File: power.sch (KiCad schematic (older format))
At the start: 3 parts

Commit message: LiPo recharge circuit
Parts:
- added C? (x2): 4.7u, symbol C
- added D?: LED, symbol LED
- added D?: MBRA140, symbol D_Schottky_Small
- added R?: 330, symbol R
- added R?: 2k, symbol R
- added U?: MCP73831, symbol MCP73831
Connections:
- net labels added: +BATT, V_USB
- wire segments 8 -> 27
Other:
- note added: "Allows to recharge \na 1 cell LiPo at 500mA\n\nIreg = 1000V/Rprog"
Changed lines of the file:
@@
 $EndComp
 Wire Wire Line
-	7600 1850 7600 1950
+	7600 1850 7600 1900
+Wire Wire Line
+	7600 1900 7600 1950
 Wire Wire Line
 	7600 1900 8150 1900
@@
 	9550 1950 9550 1900
 Wire Wire Line
-	9350 1900 9750 1900
+	9350 1900 9550 1900
+Wire Wire Line
+	9550 1900 9750 1900
 NoConn ~ 9350 2100
 Text Label 8100 2100 2    39   ~ 0
@@
 Text Notes 8200 1550 0    39   ~ 0
 3.3V to 2.8V linear regulator\nUsed to power the TOF sensor VL6180\nSee sensors sheet
+$Comp
+L MCP73831 U?
+U 1 1 5537ACF5
+P 3650 2050
+F 0 "U?" H 3400 1800 60  0000 C CNN
+F 1 "MCP73831" H 3650 2300 60  0000 C CNN
+F 2 "" H 3500 2000 60  0000 C CNN
+F 3 "" H 3500 2000 60  0000 C CNN
+	1    3650 2050
+	1    0    0    -1
+$EndComp
+$Comp
+L R R?
+U 1 1 5537AD64
+P 2950 2300
+F 0 "R?" V 3030 2300 50  0000 C CNN
+F 1 "330" V 2950 2300 50  0000 C CNN
+F 2 "" V 2880 2300 30  0000 C CNN
+F 3 "" H 2950 2300 30  0000 C CNN
+	1    2950 2300
+	1    0    0    -1
+$EndComp
+$Comp
+L LED D?
+U 1 1 5537ADFD
+P 2650 2250
+F 0 "D?" H 2650 2350 50  0000 C CNN
+F 1 "LED" H 2650 2150 50  0000 C CNN
+F 2 "" H 2650 2250 60  0000 C CNN
+F 3 "" H 2650 2250 60  0000 C CNN
+	1    2650 2250
+	0    1    1    0
+$EndComp
+$Comp
+L C C?
+U 1 1 5537AE4E
+P 2250 2200
+F 0 "C?" H 2275 2300 50  0000 L CNN
+F 1 "4.7u" H 2275 2100 50  0000 L CNN
+F 2 "" H 2288 2050 30  0000 C CNN
+F 3 "" H 2250 2200 60  0000 C CNN
+	1    2250 2200
+	1    0    0    -1
+$EndComp
+$Comp
+L C C?
+U 1 1 5537AEAE
+P 4850 2200
+F 0 "C?" H 4875 2300 50  0000 L CNN
+F 1 "4.7u" H 4875 2100 50  0000 L CNN
+F 2 "" H 4888 2050 30  0000 C CNN
+F 3 "" H 4850 2200 60  0000 C CNN
+	1    4850 2200
+	1    0    0    -1
+$EndComp
+$Comp
+L R R?
+U 1 1 5537AEF0
+P 4500 2200
+F 0 "R?" V 4580 2200 50  0000 C CNN
+F 1 "2k" V 4500 2200 50  0000 C CNN
+F 2 "" V 4430 2200 30  0000 C CNN
+F 3 "" H 4500 2200 30  0000 C CNN
+	1    4500 2200
+	1    0    0    -1
+$EndComp
+Text Notes 3300 2700 0    39   ~ 0
+Allows to recharge \na 1 cell LiPo at 500mA\n\nIreg = 1000V/Rprog
+$Comp
+L D_Schottky_Small D?
+U 1 1 5537AF42
+P 1950 1950
+F 0 "D?" H 1900 2030 50  0000 L CNN
+F 1 "MBRA140" H 1750 1850 50  0000 L CNN
+F 2 "" V 1950 1950 60  0000 C CNN
+F 3 "" V 1950 1950 60  0000 C CNN
+	1    1950 1950
+	1    0    0    -1
+$EndComp
+Wire Wire Line
+	2650 2450 2950 2450
+Wire Wire Line
+	2950 2150 3150 2150
+Wire Wire Line
+	2050 1950 2250 1950
+Wire Wire Line
+	2250 1950 2650 1950
+Wire Wire Line
+	2650 1950 3300 1950
+Wire Wire Line
+	2650 1950 2650 2050
+Wire Wire Line
+	2250 1950 2250 2050
+Connection ~ 2650 1950
+$Comp
+L GND #PWR?
+U 1 1 5537B1A6
+P 2250 2450
+F 0 "#PWR?" H 2250 2200 50  0001 C CNN
+F 1 "GND" H 2250 2300 50  0000 C CNN
+F 2 "" H 2250 2450 60  0000 C CNN
+F 3 "" H 2250 2450 60  0000 C CNN
+	1    2250 2450
+	1    0    0    -1
+$EndComp
+Wire Wire Line
+	2250 2450 2250 2350
+Connection ~ 2250 1950
+Text Label 1650 1950 2    39   ~ 0
+V_USB
+Wire Wire Line
+	1650 1950 1850 1950
+Wire Wire Line
+	4150 1950 4850 1950
+Wire Wire Line
+	4850 1900 4850 1950
+Wire Wire Line
+	4850 1950 4850 2050
+Connection ~ 4850 1950
+$Comp
+L +BATT #PWR?
+U 1 1 5537B71D
+P 4850 1900
+F 0 "#PWR?" H 4850 1750 50  0001 C CNN
+F 1 "+BATT" H 4850 2040 50  0000 C CNN
+F 2 "" H 4850 1900 60  0000 C CNN
+F 3 "" H 4850 1900 60  0000 C CNN
+	1    4850 1900
+	1    0    0    -1
+$EndComp
+$Comp
+L GND #PWR?
+U 1 1 5537B792
+P 4850 2450
+F 0 "#PWR?" H 4850 2200 50  0001 C CNN
+F 1 "GND" H 4850 2300 50  0000 C CNN
+F 2 "" H 4850 2450 60  0000 C CNN
+F 3 "" H 4850 2450 60  0000 C CNN
+	1    4850 2450
+	1    0    0    -1
+$EndComp
+Wire Wire Line
+	4850 2450 4850 2350
+$Comp
+L GND #PWR?
+U 1 1 5537B7FF
+P 4500 2400
+F 0 "#PWR?" H 4500 2150 50  0001 C CNN
+F 1 "GND" H 4500 2250 50  0000 C CNN
+F 2 "" H 4500 2400 60  0000 C CNN
+F 3 "" H 4500 2400 60  0000 C CNN
+	1    4500 2400
+	1    0    0    -1
+$EndComp
+Wire Wire Line
+	4500 2400 4500 2350
+Wire Wire Line
+	4500 2050 4150 2050
+$Comp
+L GND #PWR?
+U 1 1 5537B8E3
+P 4250 2250
+F 0 "#PWR?" H 4250 2000 50  0001 C CNN
+F 1 "GND" H 4250 2100 50  0000 C CNN
+F 2 "" H 4250 2250 60  0000 C CNN
+F 3 "" H 4250 2250 60  0000 C CNN
+	1    4250 2250
+	1    0    0    -1
+$EndComp
+Wire Wire Line
+	4250 2250 4250 2150
+Wire Wire Line
+	4250 2150 4150 2150
 $EndSCHEMATC

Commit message: Update schematic labels to handle hierarchical signal dependencies
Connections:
- net labels added: +2.8V, +2.8V_EN
- net labels removed: 2.8V, 2.8V_EN
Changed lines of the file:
@@
 	9550 1900 9750 1900
 NoConn ~ 9350 2100
-Text Label 8100 2100 2    39   ~ 0
-2.8V_EN
 Wire Wire Line
 	8100 2100 8150 2100
@@
 Wire Wire Line
 	7600 2300 7600 2250
-Text Label 9750 1900 0    39   ~ 0
-2.8V
 Connection ~ 9550 1900
 $Comp
@@
 	2250 2450 2250 2350
 Connection ~ 2250 1950
-Text Label 1650 1950 2    39   ~ 0
-V_USB
 Wire Wire Line
 	1650 1950 1850 1950
@@
 Wire Wire Line
 	4250 2150 4150 2150
+Text HLabel 1650 1950 0    39   Input ~ 0
+V_USB
+Text HLabel 8100 2100 0    39   Input ~ 0
++2.8V_EN
+Text HLabel 9750 1900 2    39   Input ~ 0
++2.8V
 $EndSCHEMATC

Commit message: Add principal power supply
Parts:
- removed C? (x2): 1u, symbol C
- removed U?: ADP150-2.8, symbol ADP150-2.8
- added C? (x2): 10u, symbol C
- added C?: 100u, symbol C
- added R?: 3.3k, symbol R
- added R?: 2.05k, symbol R
- added U?: LT1965, MODULE, symbol LT1965
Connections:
- net labels removed: +2.8V, +2.8V_EN
- wire segments 27 -> 37
- no-connect marks 1 -> 0
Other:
- note added: "V_OUT = 1.20V x (1+ R2/R1) + 1.7uA x R2 @25°C"
- note removed: "3.3V to 2.8V linear regulator\nUsed to power the TOF sensor VL6180\nSee sensors sheet"
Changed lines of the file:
@@
 $EndDescr
-$Comp
-L ADP150-2.8 U?
-U 1 1 5537A222
-P 8750 2100
-F 0 "U?" H 9000 1850 59  0000 C CNN
-F 1 "ADP150-2.8" H 8750 2450 59  0000 C CNN
-F 2 "" H 8650 2100 39  0000 C CNN
-F 3 "" H 8650 2100 39  0000 C CNN
-	1    8750 2100
-	1    0    0    -1
-$EndComp
-$Comp
-L C C?
-U 1 1 5537A275
-P 7600 2100
-F 0 "C?" H 7625 2200 50  0000 L CNN
-F 1 "1u" H 7625 2000 50  0000 L CNN
-F 2 "" H 7638 1950 30  0000 C CNN
-F 3 "" H 7600 2100 60  0000 C CNN
-	1    7600 2100
-	1    0    0    -1
-$EndComp
-$Comp
-L C C?
-U 1 1 5537A2AC
-P 9550 2100
-F 0 "C?" H 9575 2200 50  0000 L CNN
-F 1 "1u" H 9575 2000 50  0000 L CNN
-F 2 "" H 9588 1950 30  0000 C CNN
-F 3 "" H 9550 2100 60  0000 C CNN
-	1    9550 2100
-	1    0    0    -1
-$EndComp
-$Comp
-L GND #PWR?
-U 1 1 5537A2E3
-P 8750 2650
-F 0 "#PWR?" H 8750 2400 50  0001 C CNN
-F 1 "GND" H 8750 2500 50  0000 C CNN
-F 2 "" H 8750 2650 60  0000 C CNN
-F 3 "" H 8750 2650 60  0000 C CNN
-	1    8750 2650
-	1    0    0    -1
-$EndComp
-Wire Wire Line
-	8750 2650 8750 2600
-$Comp
-L VCC #PWR?
-U 1 1 5537A2FF
-P 7600 1850
-F 0 "#PWR?" H 7600 1700 50  0001 C CNN
-F 1 "VCC" H 7600 2000 50  0000 C CNN
-F 2 "" H 7600 1850 60  0000 C CNN
-F 3 "" H 7600 1850 60  0000 C CNN
-	1    7600 1850
-	1    0    0    -1
-$EndComp
-Wire Wire Line
-	7600 1850 7600 1900
-Wire Wire Line
-	7600 1900 7600 1950
-Wire Wire Line
-	7600 1900 8150 1900
-Connection ~ 7600 1900
-Wire Wire Line
-	9550 1950 9550 1900
-Wire Wire Line
-	9350 1900 9550 1900
-Wire Wire Line
-	9550 1900 9750 1900
-NoConn ~ 9350 2100
-Wire Wire Line
-	8100 2100 8150 2100
-$Comp
-L GND #PWR?
-U 1 1 5537A3AB
-P 7600 2300
-F 0 "#PWR?" H 7600 2050 50  0001 C CNN
-F 1 "GND" H 7600 2150 50  0000 C CNN
-F 2 "" H 7600 2300 60  0000 C CNN
-F 3 "" H 7600 2300 60  0000 C CNN
-	1    7600 2300
-	1    0    0    -1
-$EndComp
-Wire Wire Line
-	7600 2300 7600 2250
-Connection ~ 9550 1900
-$Comp
-L GND #PWR?
-U 1 1 5537A3FA
-P 9550 2300
-F 0 "#PWR?" H 9550 2050 50  0001 C CNN
-F 1 "GND" H 9550 2150 50  0000 C CNN
-F 2 "" H 9550 2300 60  0000 C CNN
-F 3 "" H 9550 2300 60  0000 C CNN
-	1    9550 2300
-	1    0    0    -1
-$EndComp
-Wire Wire Line
-	9550 2300 9550 2250
-Text Notes 8200 1550 0    39   ~ 0
-3.3V to 2.8V linear regulator\nUsed to power the TOF sensor VL6180\nSee sensors sheet
 $Comp
 L MCP73831 U?
@@
 	1    0    0    -1
 $EndComp
-Wire Wire Line
-	2650 2450 2950 2450
-Wire Wire Line
-	2950 2150 3150 2150
-Wire Wire Line
-	2050 1950 2250 1950
-Wire Wire Line
-	2250 1950 2650 1950
-Wire Wire Line
-	2650 1950 3300 1950
-Wire Wire Line
-	2650 1950 2650 2050
-Wire Wire Line
-	2250 1950 2250 2050
-Connection ~ 2650 1950
 $Comp
 L GND #PWR?
@@
 	1    0    0    -1
 $EndComp
-Wire Wire Line
-	2250 2450 2250 2350
-Connection ~ 2250 1950
-Wire Wire Line
-	1650 1950 1850 1950
-Wire Wire Line
-	4150 1950 4850 1950
-Wire Wire Line
-	4850 1900 4850 1950
-Wire Wire Line
-	4850 1950 4850 2050
-Connection ~ 4850 1950
 $Comp
 L +BATT #PWR?
@@
 	1    0    0    -1
 $EndComp
-Wire Wire Line
-	4850 2450 4850 2350
 $Comp
 L GND #PWR?
@@
 	1    0    0    -1
 $EndComp
-Wire Wire Line
-	4500 2400 4500 2350
-Wire Wire Line
-	4500 2050 4150 2050
 $Comp
 L GND #PWR?
@@
 	1    0    0    -1
 $EndComp
-Wire Wire Line
-	4250 2250 4250 2150
-Wire Wire Line
-	4250 2150 4150 2150
 Text HLabel 1650 1950 0    39   Input ~ 0
 V_USB
-Text HLabel 8100 2100 0    39   Input ~ 0
-+2.8V_EN
-Text HLabel 9750 1900 2    39   Input ~ 0
-+2.8V
+$Comp
+L LT1965 U?
+U 1 1 55383A0A
+P 8100 2150
+F 0 "U?" H 8450 2450 50  0000 C CNN
+F 1 "LT1965" H 7850 2450 50  0000 C CNN
+F 2 "MODULE" H 8100 2250 50  0001 C CNN
+F 3 "DOCUMENTATION" H 8100 2250 50  0001 C CNN
+	1    8100 2150
+	1    0    0    -1
+$EndComp
+$Comp
+L GND #PWR?
+U 1 1 55383A83
+P 8200 2750
+F 0 "#PWR?" H 8200 2500 50  0001 C CNN
+F 1 "GND" H 8200 2600 50  0000 C CNN
+F 2 "" H 8200 2750 60  0000 C CNN
+F 3 "" H 8200 2750 60  0000 C CNN
+	1    8200 2750
+	1    0    0    -1
+$EndComp
+$Comp
+L +BATT #PWR?
+U 1 1 55383BBD
+P 6850 1950
+F 0 "#PWR?" H 6850 1800 50  0001 C CNN
+F 1 "+BATT" H 6850 2090 50  0000 C CNN
+F 2 "" H 6850 1950 60  0000 C CNN
+F 3 "" H 6850 1950 60  0000 C CNN
+	1    6850 1950
+	1    0    0    -1
+$EndComp
+$Comp
+L VCC #PWR?
+U 1 1 55383BD9
+P 9350 1950
+F 0 "#PWR?" H 9350 1800 50  0001 C CNN
+F 1 "VCC" H 9350 2100 50  0000 C CNN
+F 2 "" H 9350 1950 60  0000 C CNN
+F 3 "" H 9350 1950 60  0000 C CNN
+	1    9350 1950
+	1    0    0    -1
+$EndComp
+Text Notes 7300 1700 0    39   ~ 0
+V_OUT = 1.20V x (1+ R2/R1) + 1.7uA x R2  @25°C
+$Comp
+L R R?
+U 1 1 55383C72
+P 9000 2200
+F 0 "R?" V 9080 2200 50  0000 C CNN
+F 1 "3.3k" V 9000 2200 50  0000 C CNN
+F 2 "" V 8930 2200 30  0000 C CNN
+F 3 "" H 9000 2200 30  0000 C CNN
+	1    9000 2200
+	1    0    0    -1
+$EndComp
+$Comp
+L R R?
+U 1 1 55383CC5
+P 9000 2600
+F 0 "R?" V 9080 2600 50  0000 C CNN
+F 1 "2.05k" V 9000 2600 50  0000 C CNN
+F 2 "" V 8930 2600 30  0000 C CNN
+F 3 "" H 9000 2600 30  0000 C CNN
+	1    9000 2600
+	1    0    0    -1
+$EndComp
+$Comp
+L GND #PWR?
+U 1 1 55383E55
+P 9000 2750
+F 0 "#PWR?" H 9000 2500 50  0001 C CNN
+F 1 "GND" H 9000 2600 50  0000 C CNN
+F 2 "" H 9000 2750 60  0000 C CNN
+F 3 "" H 9000 2750 60  0000 C CNN
+	1    9000 2750
+	1    0    0    -1
+$EndComp
+$Comp
+L C C?
+U 1 1 55384138
+P 9350 2250
+F 0 "C?" H 9375 2350 50  0000 L CNN
+F 1 "10u" H 9375 2150 50  0000 L CNN
+F 2 "" H 9388 2100 30  0000 C CNN
+F 3 "" H 9350 2250 60  0000 C CNN
+	1    9350 2250
+	1    0    0    -1
+$EndComp
+$Comp
+L C C?
+U 1 1 55384192
+P 7100 2250
+F 0 "C?" H 7125 2350 50  0000 L CNN
+F 1 "10u" H 7125 2150 50  0000 L CNN
+F 2 "" H 7138 2100 30  0000 C CNN
+F 3 "" H 7100 2250 60  0000 C CNN
+	1    7100 2250
+	1    0    0    -1
+$EndComp
+$Comp
+L C C?
+U 1 1 553841EE
+P 6850 2250
+F 0 "C?" H 6875 2350 50  0000 L CNN
+F 1 "100u" H 6875 2150 50  0000 L CNN
+F 2 "" H 6888 2100 30  0000 C CNN
+F 3 "" H 6850 2250 60  0000 C CNN
+	1    6850 2250
+	1    0    0    -1
+$EndComp
+$Comp
+L GND #PWR?
+U 1 1 553845EA
+P 9350 2500
+F 0 "#PWR?" H 9350 2250 50  0001 C CNN
+F 1 "GND" H 9350 2350 50  0000 C CNN
+F 2 "" H 9350 2500 60  0000 C CNN
+F 3 "" H 9350 2500 60  0000 C CNN
+	1    9350 2500
+	1    0    0    -1
+$EndComp
+$Comp
+L GND #PWR?
+U 1 1 5538464A
+P 6850 2500
+F 0 "#PWR?" H 6850 2250 50  0001 C CNN
+F 1 "GND" H 6850 2350 50  0000 C CNN
+F 2 "" H 6850 2500 60  0000 C CNN
+F 3 "" H 6850 2500 60  0000 C CNN
+	1    6850 2500
+	1    0    0    -1
+$EndComp
+Wire Wire Line
+	2650 2450 2950 2450
+Wire Wire Line
+	2950 2150 3150 2150
+Wire Wire Line
+	2050 1950 3300 1950
+Wire Wire Line
+	2650 1950 2650 2050
+Wire Wire Line
+	2250 1950 2250 2050
+Connection ~ 2650 1950
+Wire Wire Line
+	2250 2450 2250 2350
+Connection ~ 2250 1950
+Wire Wire Line
+	1650 1950 1850 1950
+Wire Wire Line
+	4150 1950 4850 1950
+Wire Wire Line
+	4850 1900 4850 2050
+Connection ~ 4850 1950
+Wire Wire Line
+	4850 2450 4850 2350
+Wire Wire Line
+	4500 2400 4500 2350
+Wire Wire Line
+	4500 2050 4150 2050
+Wire Wire Line
+	4250 2250 4250 2150
+Wire Wire Line
+	4250 2150 4150 2150
+Wire Wire Line
+	8200 2650 8200 2750
+Wire Wire Line
+	8100 2650 8100 2700
+Wire Wire Line
+	8000 2700 8200 2700
+Connection ~ 8200 2700
+Wire Wire Line
+	8000 2700 8000 2650
+Connection ~ 8100 2700
+Wire Wire Line
+	8700 2100 8750 2100
+Wire Wire Line
+	8750 2100 8750 2000
+Wire Wire Line
+	8700 2000 9350 2000
+Wire Wire Line
+	9000 2000 9000 2050
+Connection ~ 8750 2000
+Connection ~ 9000 2000
+Wire Wire Line
+	9000 2350 9000 2450
+Wire Wire Line
+	9000 2400 8750 2400
+Wire Wire Line
+	8750 2400 8750 2200
+Wire Wire Line
+	8750 2200 8700 2200
+Connection ~ 9000 2400
+Wire Wire Line
+	9350 1950 9350 2100
+Wire Wire Line
+	6850 1950 6850 2100
+Wire Wire Line
+	6850 2000 7500 2000
+Connection ~ 6850 2000
+Wire Wire Line
+	7500 2100 7450 2100
+Wire Wire Line
+	7450 2000 7450 2200
+Connection ~ 7450 2000
+Wire Wire Line
+	7100 2100 7100 2000
+Connection ~ 7100 2000
+Connection ~ 9350 2000
+Wire Wire Line
+	9350 2500 9350 2400
+Wire Wire Line
+	6850 2400 6850 2500
+Wire Wire Line
+	7100 2400 7100 2450
+Wire Wire Line
+	7100 2450 6850 2450
+Connection ~ 6850 2450
+Wire Wire Line
+	7450 2200 7500 2200
+Connection ~ 7450 2100
 $EndSCHEMATC

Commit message: Motors & drivers TI drv8839 (independent pwm) added to schematics
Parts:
- added C? (x2): 0.1, symbol C
- added C? (x2): 10u, symbol C
- added CONN?: MOTOR_1, MODULE, symbol PWR
- added CONN?: MOTOR_2, MODULE, symbol PWR
- added CONN?: MOTOR_3, MODULE, symbol PWR
- added CONN?: MOTOR_4, MODULE, symbol PWR
- added U? (x2): DRV8839, symbol DRV8839
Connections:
- net labels added: MOTOR_1_EN, MOTOR_1_IN, MOTOR_1_OUT, MOTOR_2_EN, MOTOR_2_IN, MOTOR_2_OUT, MOTOR_3_EN, MOTOR_3_IN, MOTOR_3_OUT, MOTOR_4_EN, MOTOR_4_IN, MOTOR_4_OUT
- wire segments 37 -> 85
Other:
- moved on the sheet: D?, R?, U?

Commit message: nRF24L01+ integrated + correct capacitors
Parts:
- removed C? (x2): 4.7u, symbol C
- removed C? (x4): 10u, symbol C
- removed C?: 100u, symbol C
- removed C? (x2): 0.1, symbol C
- added C? (x2): 4.7uF, symbol C_Small
- added C? (x4): 10uF, symbol C_Small
- added C?: 100uF, symbol C_Small
- added C? (x2): 0.1uF, symbol C_Small
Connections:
- wire segments 85 -> 108
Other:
- moved on the sheet: D?, R?

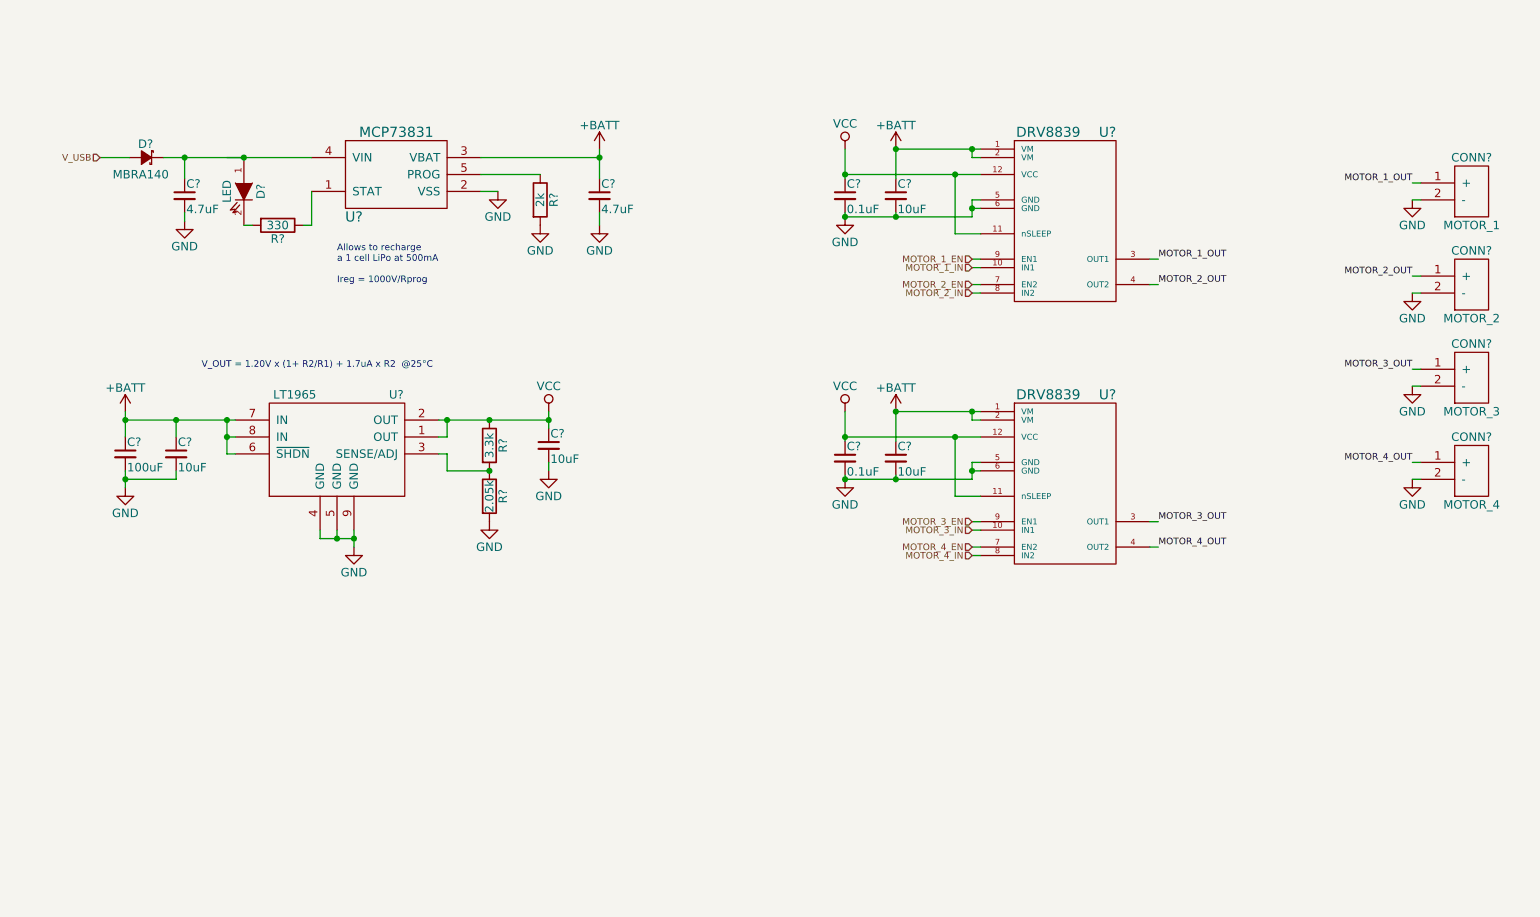
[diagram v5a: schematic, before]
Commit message: Move nrf24 to separate sheet and Add USB termination
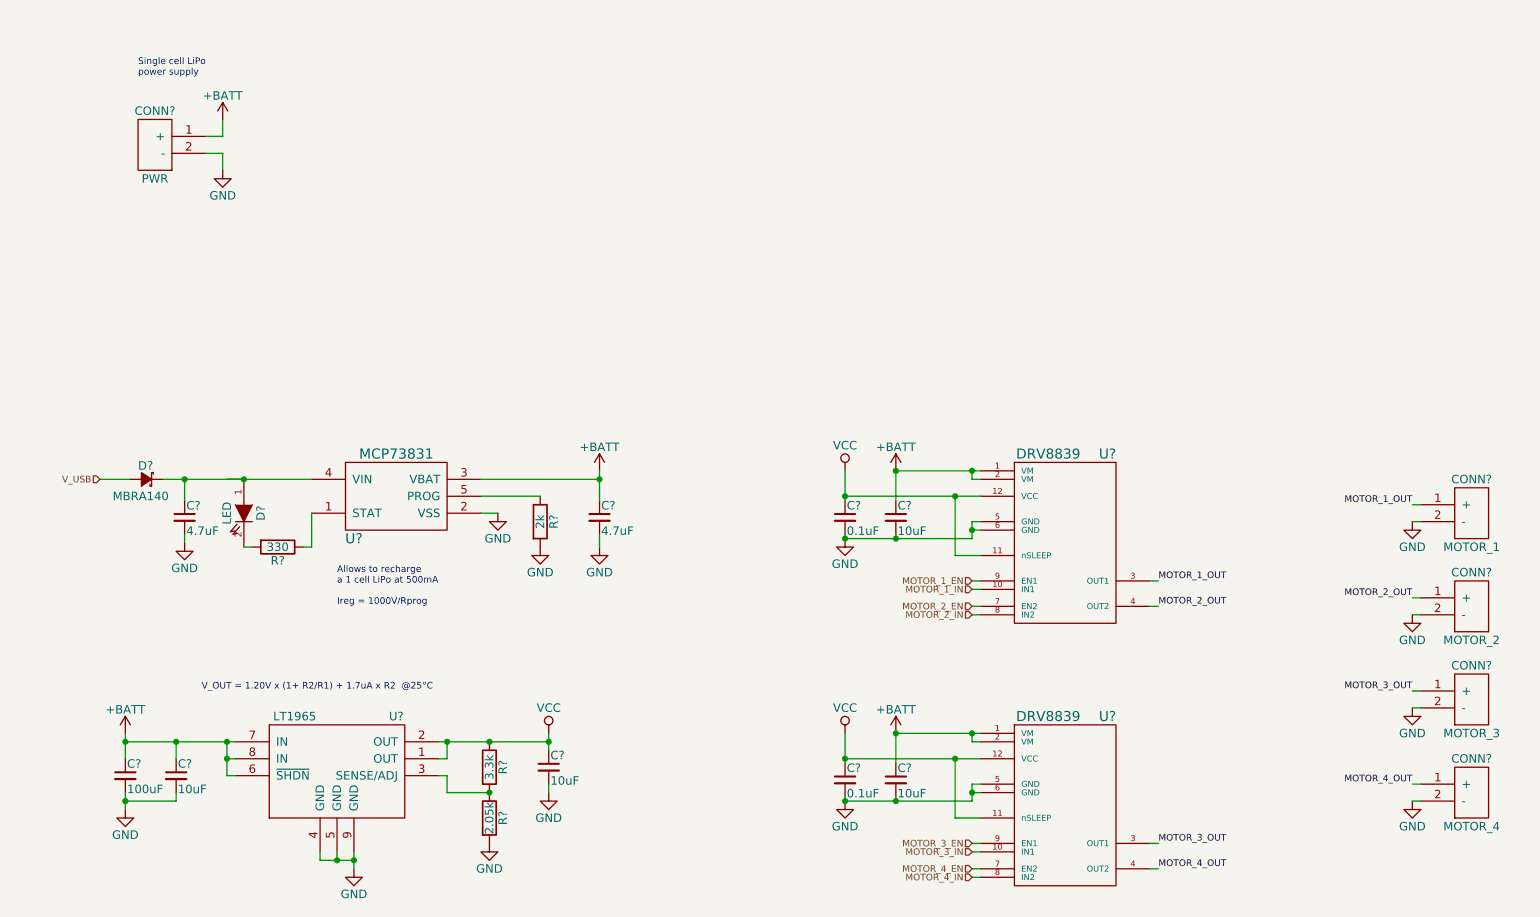
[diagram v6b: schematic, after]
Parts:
- added CONN?: PWR, MODULE, symbol PWR
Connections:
- net +BATT: now also CONN?.1 (+)
- net GND: now also CONN?.2 (-), CONN?.MECH (GND)
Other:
- note added: "Single cell LiPo \npower supply\n"
- moved on the sheet: C?, CONN?, D?, R?, U?
